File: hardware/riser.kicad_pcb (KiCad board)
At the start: 2 copper layers, 46.5 x 63.5 mm, 1 part

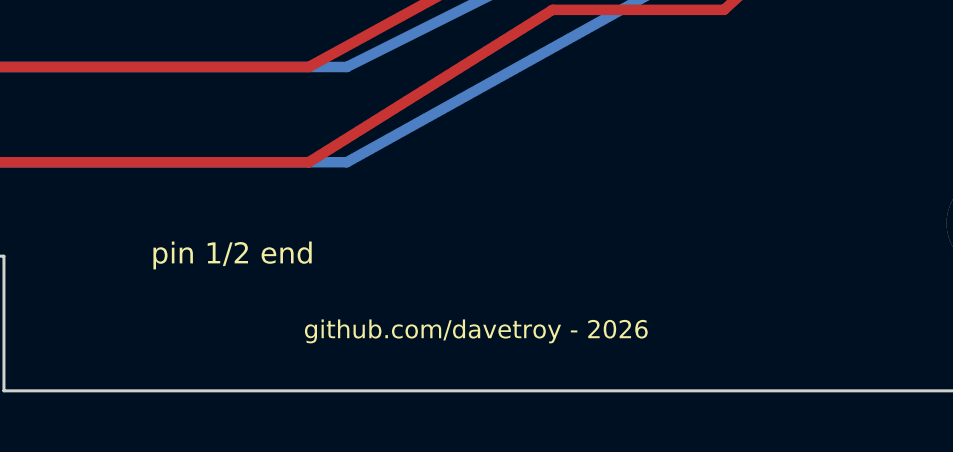
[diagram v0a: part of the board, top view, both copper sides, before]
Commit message: Order prep: memorial notice on both boards, ORDER.md package
Both boards now carry "(c) 2026 David Troy, in memory of Stephen
Troy." on the silkscreen — the card along its bottom edge, the riser
on two lines. Regenerated boards, fab zips, gerbers, and 1:1 plots;
re-verified DRC-clean (0 violations, 0 unconnected on both). ORDER.md
carries the full PCBWay parameter set, the pre-upload checklist, the
per-card BOM, and the bring-up sequence for when the boards arrive.

Co-Authored-By: Claude Fable 5 <noreply@anthropic.com>
Claude-Session: https://claude.ai/code/session_01PB6zhL6oFB9zbtD4W85UDt
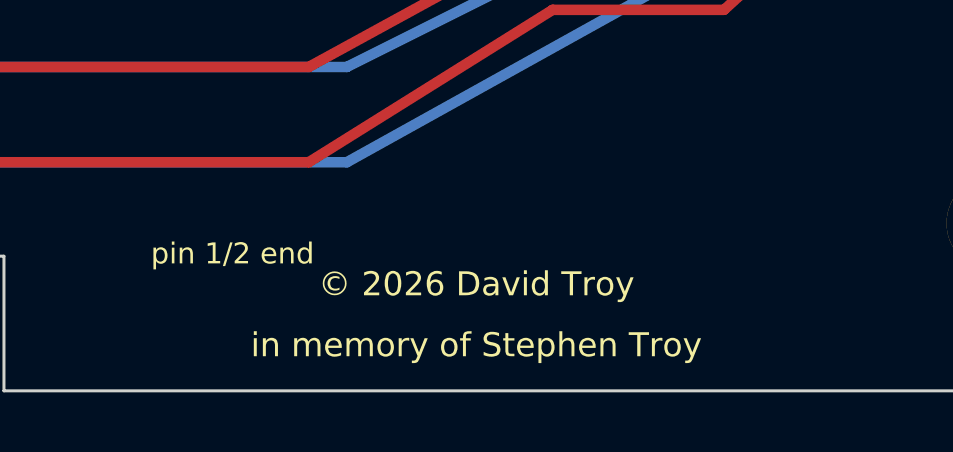
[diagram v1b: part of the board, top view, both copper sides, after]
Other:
- board text added: "in memory of Stephen Troy"
- board text added: "© 2026 David Troy"
- board text removed: "github.com/davetroy - 2026"
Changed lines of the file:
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@@
   (gr_text "pin 1/2 end" (at 7.62 58.928) (layer "F.SilkS") (effects (font (size 0.7 0.7) (thickness 0.15))))
   (gr_text "pin 29/30 end" (at 7.62 13.208) (layer "F.SilkS") (effects (font (size 0.7 0.7) (thickness 0.15))))
-  (gr_text "github.com/davetroy - 2026" (at 15.748 61.468) (layer "F.SilkS") (effects (font (size 0.6 0.6) (thickness 0.15))))
+  (gr_text "© 2026 David Troy" (at 15.748 59.944) (layer "F.SilkS") (effects (font (size 0.8 0.8) (thickness 0.15))))
+  (gr_text "in memory of Stephen Troy" (at 15.748 61.976) (layer "F.SilkS") (effects (font (size 0.8 0.8) (thickness 0.15))))
   (segment (start -0.508 55.88) (end 10.16 55.88) (width 0.35) (layer "F.Cu") (net 2))
   (segment (start 10.16 55.88) (end 18.288 50.8) (width 0.35) (layer "F.Cu") (net 2))
